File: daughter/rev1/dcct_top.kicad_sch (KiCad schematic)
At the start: 20 parts, among them U20 LT3042xMSE, U32 LTC6655BHLS8-5, U35 LT6202CS5

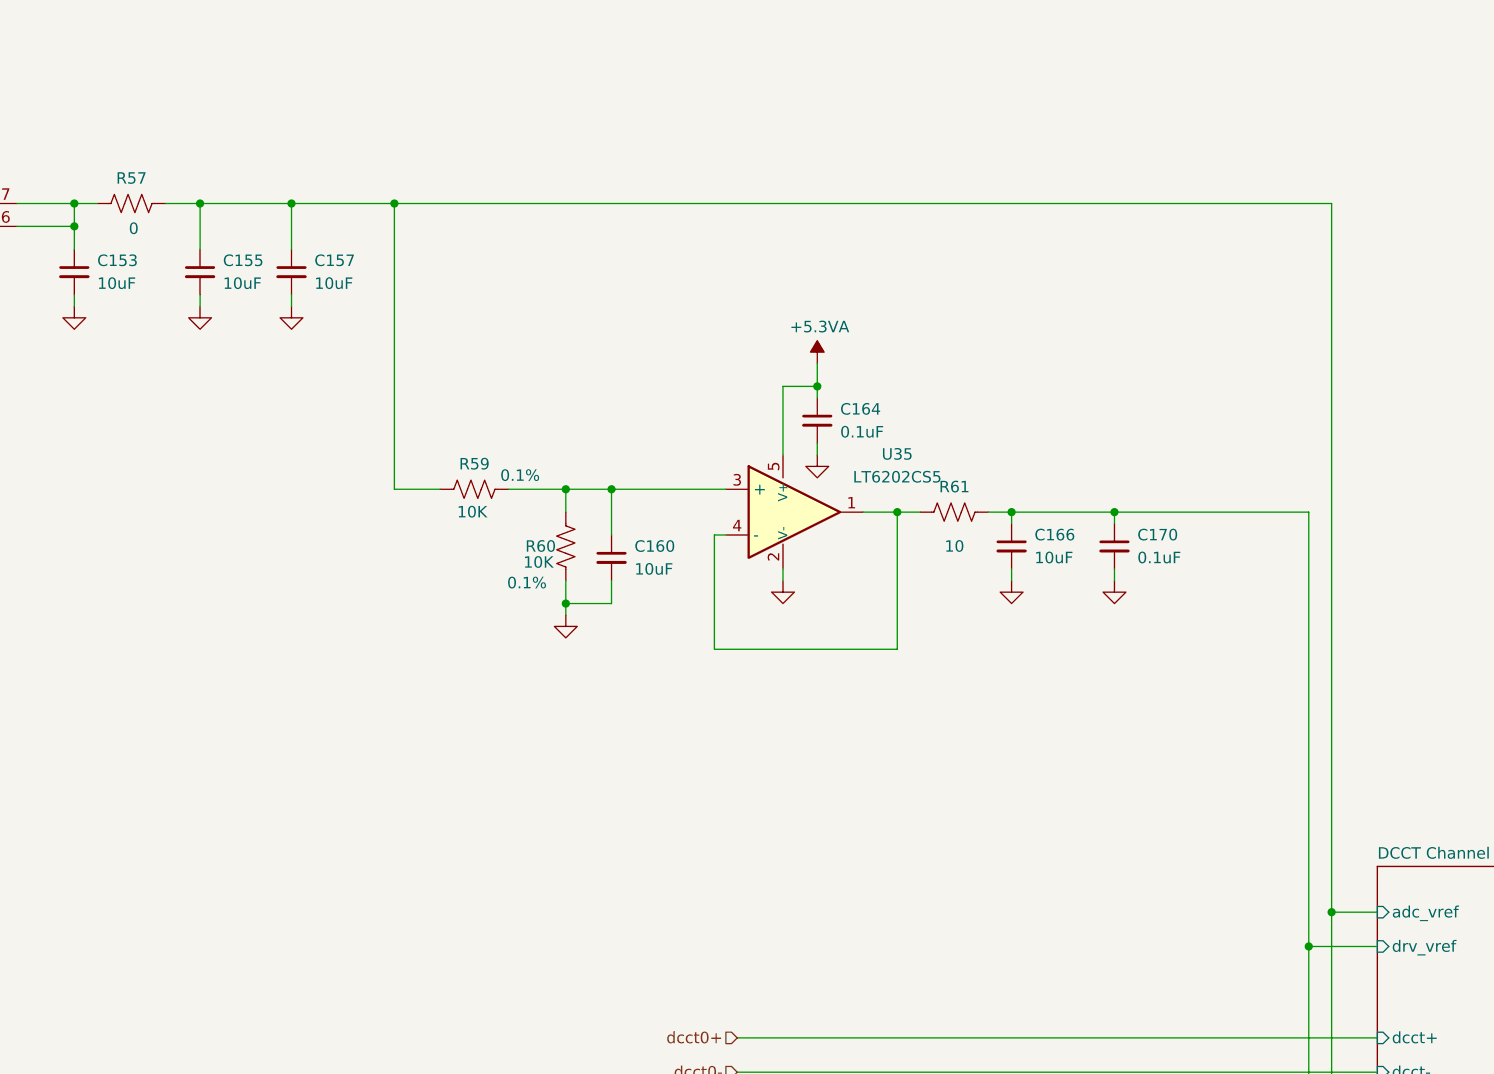
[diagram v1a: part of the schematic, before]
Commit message: linked ADR1001 to DCCT ADC reference for 5V and 2.5V
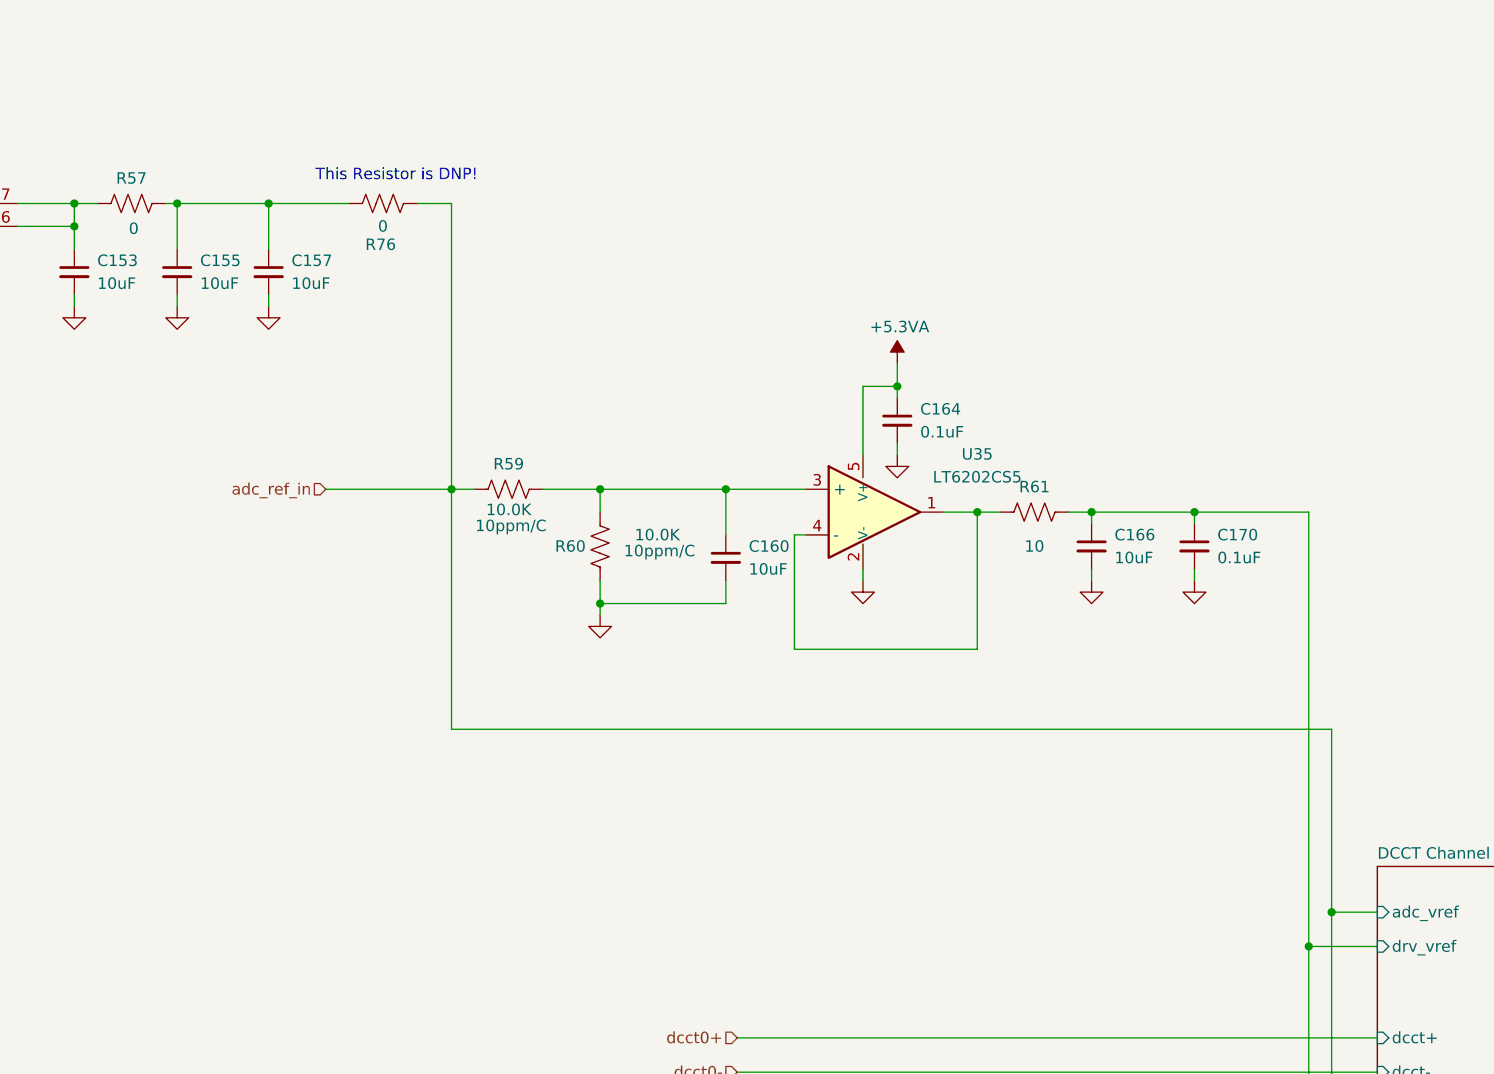
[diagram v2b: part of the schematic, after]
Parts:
- added R76: 0, Resistor_SMD:R_0402_1005Metric, symbol Device:R_US
- R59, R60: value 10K -> 10.0K; footprint Resistor_SMD:R_0402_1005Metric -> Resistor_SMD:R_0603_1608Metric; MFG Panasonic -> Yageo; MFG_PN ERJ-2RKF1002X -> RT0603BRB0710KL; PPM (none) -> 10ppm/C
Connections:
- net GND: now also R60.1; no longer R60.2
- net at C160.1, R59.1, U35.3 (+): now also R60.2; no longer R60.1
- net DCCT Channel 1/adc_vref: no longer names the net of C155.1, C157.1, R57.1
- net DCCT Channel 1/adc_vref: now also R76.1; no longer R59.2
- new net adc_ref_in: R59.2, R76.2
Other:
- note added: "This Resistor is DNP!"
- moved on the sheet: C155, C157, C160, C164, C166, C170, R61, U35

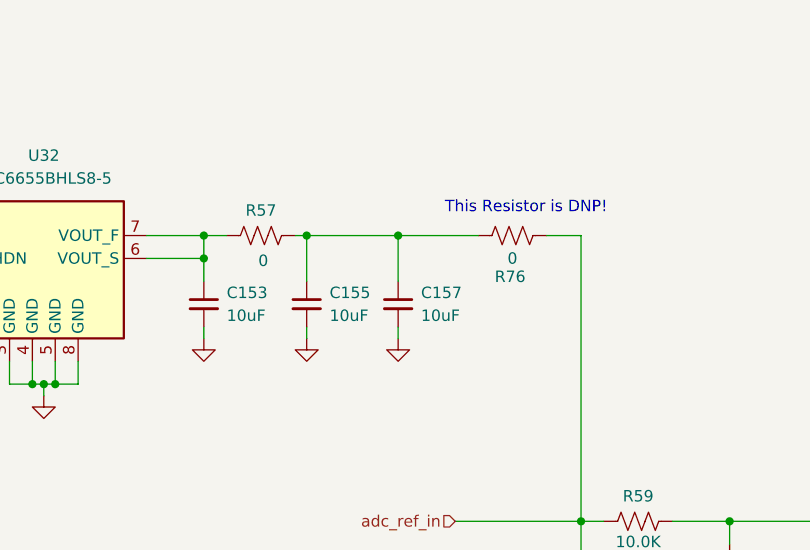
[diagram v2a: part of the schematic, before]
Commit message: Finish routing of daughterboard
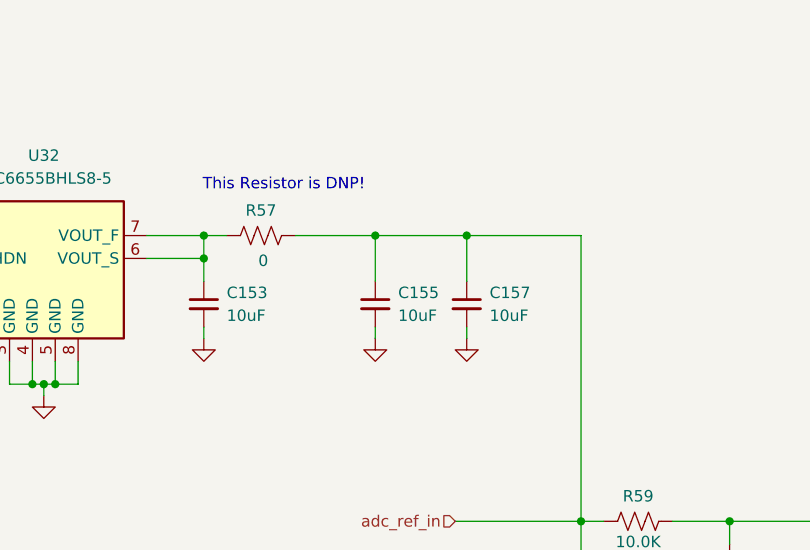
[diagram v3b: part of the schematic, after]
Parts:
- removed R76: 0, Resistor_SMD:R_0402_1005Metric, symbol Device:R_US
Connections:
- net adc_ref_in: now also C155.1, C157.1, R57.1
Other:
- moved on the sheet: C155, C157
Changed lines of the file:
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@@
 	(text "This Resistor is DNP!\n"
 		(exclude_from_sim no)
-		(at 162.814 46.482 0)
+		(at 135.89 43.942 0)
 		(effects
 			(font
@@
 	)
 	(junction
-		(at 148.59 49.53)
-		(diameter 0)
-		(color 0 0 0 0)
-	)
-	(junction
 		(at 96.52 49.53)
 		(diameter 0)
@@
 	)
 	(junction
+		(at 146.05 49.53)
+		(diameter 0)
+		(color 0 0 0 0)
+	)
+	(junction
 		(at 50.8 49.53)
 		(diameter 0)
@@
 	)
 	(junction
-		(at 138.43 49.53)
+		(at 156.21 49.53)
 		(diameter 0)
 		(color 0 0 0 0)
@@
 	(wire
 		(pts
-			(xy 138.43 49.53) (xy 148.59 49.53)
+			(xy 146.05 49.53) (xy 156.21 49.53)
 		)
 		(stroke
@@
 	(wire
 		(pts
-			(xy 148.59 60.96) (xy 148.59 59.69)
+			(xy 156.21 60.96) (xy 156.21 59.69)
 		)
 		(stroke
@@
 	(wire
 		(pts
-			(xy 138.43 60.96) (xy 138.43 59.69)
+			(xy 146.05 60.96) (xy 146.05 59.69)
 		)
 		(stroke
@@
 	(wire
 		(pts
-			(xy 137.16 49.53) (xy 138.43 49.53)
-		)
-		(stroke
-			(width 0)
-			(type default)
-		)
-	)
-	(wire
-		(pts
 			(xy 179.07 81.28) (xy 185.42 81.28)
 		)
@@
 	(wire
 		(pts
-			(xy 165.1 49.53) (xy 168.91 49.53)
-		)
-		(stroke
-			(width 0)
-			(type default)
-		)
-	)
-	(wire
-		(pts
 			(xy 50.8 52.07) (xy 53.34 52.07)
 		)
@@
 	(wire
 		(pts
-			(xy 148.59 54.61) (xy 148.59 49.53)
+			(xy 156.21 54.61) (xy 156.21 49.53)
 		)
 		(stroke
@@
 	(wire
 		(pts
+			(xy 137.16 49.53) (xy 146.05 49.53)
+		)
+		(stroke
+			(width 0)
+			(type default)
+		)
+	)
+	(wire
+		(pts
 			(xy 308.61 133.35) (xy 317.5 133.35)
 		)
@@
 	(wire
 		(pts
+			(xy 156.21 49.53) (xy 168.91 49.53)
+		)
+		(stroke
+			(width 0)
+			(type default)
+		)
+	)
+	(wire
+		(pts
 			(xy 127 60.96) (xy 127 59.69)
 		)
@@
 	(wire
 		(pts
-			(xy 138.43 49.53) (xy 138.43 54.61)
+			(xy 146.05 49.53) (xy 146.05 54.61)
 		)
 		(stroke
@@
 	(wire
 		(pts
-			(xy 148.59 49.53) (xy 157.48 49.53)
-		)
-		(stroke
-			(width 0)
-			(type default)
-		)
-	)
-	(wire
-		(pts
 			(xy 97.79 52.07) (xy 96.52 52.07)
 		)
@@
 	(symbol
 		(lib_id "Device:C_Small")
-		(at 138.43 57.15 0)
+		(at 146.05 57.15 0)
 		(unit 1)
 		(exclude_from_sim no)
@@
 		(dnp no)
 		(property "Reference" "C155"
-			(at 140.97 55.8862 0)
+			(at 148.59 55.8862 0)
 			(effects
 				(font
@@
 		)
 		(property "Value" "10uF"
-			(at 140.97 58.4262 0)
+			(at 148.59 58.4262 0)
 			(effects
 				(font
@@
 		)
 		(property "Footprint" "Capacitor_SMD:C_0603_1608Metric"
-			(at 138.43 57.15 0)
+			(at 146.05 57.15 0)
 			(effects
 				(font
@@
 		)
 		(property "Datasheet" "~"
-			(at 138.43 57.15 0)
+			(at 146.05 57.15 0)
 			(effects
 				(font
@@
 		)
 		(property "Description" "CAP CER 10UF 25V X5R 0603"
-			(at 138.43 57.15 0)
+			(at 146.05 57.15 0)
 			(effects
 				(font
@@
 		)
 		(property "Voltage" "25V"
-			(at 142.748 60.706 0)
+			(at 150.368 60.706 0)
 			(effects
 				(font
@@
 		)
 		(property "MFG" "Samsung"
-			(at 138.43 57.15 0)
+			(at 146.05 57.15 0)
 			(effects
 				(font
@@
 		)
 		(property "MFG_PN" "CL10A106MA8NRNC\n"
-			(at 138.43 57.15 0)
+			(at 146.05 57.15 0)
 			(effects
 				(font
@@
 	(symbol
 		(lib_id "Device:R_US")
-		(at 161.29 49.53 90)
-		(unit 1)
-		(exclude_from_sim no)
-		(in_bom yes)
-		(on_board yes)
-		(dnp no)
-		(property "Reference" "R76"
-			(at 161.036 54.102 90)
-			(effects
-				(font
-					(size 1.27 1.27)
-				)
-			)
-		)
-		(property "Value" "0"
-			(at 161.29 52.07 90)
-			(effects
-				(font
-					(size 1.27 1.27)
-				)
-			)
-		)
-		(property "Footprint" "Resistor_SMD:R_0402_1005Metric"
-			(at 161.544 48.514 90)
-			(effects
-				(font
-					(size 1.27 1.27)
-				)
-				(hide yes)
-			)
-		)
-		(property "Datasheet" "~"
-			(at 161.29 49.53 0)
-			(effects
-				(font
-					(size 1.27 1.27)
-				)
-				(hide yes)
-			)
-		)
-		(property "Description" "RES SMD 0 OHM JUMPER 1/10W 0402"
-			(at 161.29 49.53 0)
-			(effects
-				(font
-					(size 1.27 1.27)
-				)
-				(hide yes)
-			)
-		)
-		(property "Tolerance" "1%"
-			(at 157.988 46.736 90)
-			(effects
-				(font
-					(size 1.27 1.27)
-				)
-				(hide yes)
-			)
-		)
-		(property "MFG" "Panasonic"
-			(at 161.29 49.53 90)
-			(effects
-				(font
-					(size 1.27 1.27)
-				)
-				(hide yes)
-			)
-		)
-		(property "MFG_PN" "ERJ-2GE0R00X"
-			(at 161.29 49.53 90)
-			(effects
-				(font
-					(size 1.27 1.27)
-				)
-				(hide yes)
-			)
-		)
-		(pin "2"
-		)
-		(pin "1"
-		)
-		(instances
-			(project "psc_daughter_brd"
-				(path "/40891cc8-bf64-41f4-8f69-a607d7b280eb/befff6ff-020c-4bdc-a736-6c19d2d39203"
-					(reference "R76")
-					(unit 1)
-				)
-			)
-		)
-	)
-	(symbol
-		(lib_id "Device:R_US")
 		(at 233.68 83.82 270)
 		(unit 1)
@@
 	(symbol
 		(lib_id "power:GND")
-		(at 148.59 60.96 0)
+		(at 156.21 60.96 0)
 		(unit 1)
 		(exclude_from_sim no)
@@
 		(fields_autoplaced yes)
 		(property "Reference" "#PWR0228"
-			(at 148.59 67.31 0)
+			(at 156.21 67.31 0)
 			(effects
 				(font
@@
 		)
 		(property "Value" "GND"
-			(at 148.59 66.04 0)
+			(at 156.21 66.04 0)
 			(effects
 				(font
@@
 		)
 		(property "Footprint" ""
-			(at 148.59 60.96 0)
+			(at 156.21 60.96 0)
 			(effects
 				(font
@@
 		)
 		(property "Datasheet" ""
-			(at 148.59 60.96 0)
+			(at 156.21 60.96 0)
 			(effects
 				(font
@@
 		)
 		(property "Description" "Power symbol creates a global label with name \"GND\" , ground"
-			(at 148.59 60.96 0)
+			(at 156.21 60.96 0)
 			(effects
 				(font
@@
 	(symbol
 		(lib_id "power:GND")
-		(at 138.43 60.96 0)
+		(at 146.05 60.96 0)
 		(unit 1)
 		(exclude_from_sim no)
@@
 		(fields_autoplaced yes)
 		(property "Reference" "#PWR0225"
-			(at 138.43 67.31 0)
+			(at 146.05 67.31 0)
 			(effects
 				(font
@@
 		)
 		(property "Value" "GND"
-			(at 138.43 66.04 0)
+			(at 146.05 66.04 0)
 			(effects
 				(font
@@
 		)
 		(property "Footprint" ""
-			(at 138.43 60.96 0)
+			(at 146.05 60.96 0)
 			(effects
 				(font
@@
 		)
 		(property "Datasheet" ""
-			(at 138.43 60.96 0)
+			(at 146.05 60.96 0)
 			(effects
 				(font
@@
 		)
 		(property "Description" "Power symbol creates a global label with name \"GND\" , ground"
-			(at 138.43 60.96 0)
+			(at 146.05 60.96 0)
 			(effects
 				(font
@@
 	(symbol
 		(lib_id "Device:C_Small")
-		(at 148.59 57.15 0)
+		(at 156.21 57.15 0)
 		(unit 1)
 		(exclude_from_sim no)
@@
 		(dnp no)
 		(property "Reference" "C157"
-			(at 151.13 55.8862 0)
+			(at 158.75 55.8862 0)
 			(effects
 				(font
@@
 		)
 		(property "Value" "10uF"
-			(at 151.13 58.4262 0)
+			(at 158.75 58.4262 0)
 			(effects
 				(font
@@
 		)
 		(property "Footprint" "Capacitor_SMD:C_0603_1608Metric"
-			(at 148.59 57.15 0)
+			(at 156.21 57.15 0)
 			(effects
 				(font
@@
 		)
 		(property "Datasheet" "~"
-			(at 148.59 57.15 0)
+			(at 156.21 57.15 0)
 			(effects
 				(font
@@
 		)
 		(property "Description" "CAP CER 10UF 25V X5R 0603"
-			(at 148.59 57.15 0)
+			(at 156.21 57.15 0)
 			(effects
 				(font
@@
 		)
 		(property "Voltage" "25V"
-			(at 152.908 60.706 0)
+			(at 160.528 60.706 0)
 			(effects
 				(font
@@
 		)
 		(property "MFG" "Samsung"
-			(at 148.59 57.15 0)
+			(at 156.21 57.15 0)
 			(effects
 				(font
@@
 		)
 		(property "MFG_PN" "CL10A106MA8NRNC\n"
-			(at 148.59 57.15 0)
+			(at 156.21 57.15 0)
 			(effects
 				(font
